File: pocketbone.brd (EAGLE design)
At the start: 55 x 35 mm, 61 parts, among them J1 USD_CONNECTOR, U5 24LC_32AT-I/OT, U6 SN74LVC1G07_DCK_5, Y1 CM200C-32.768KAZF-UT, Y2 445C33D24M00000

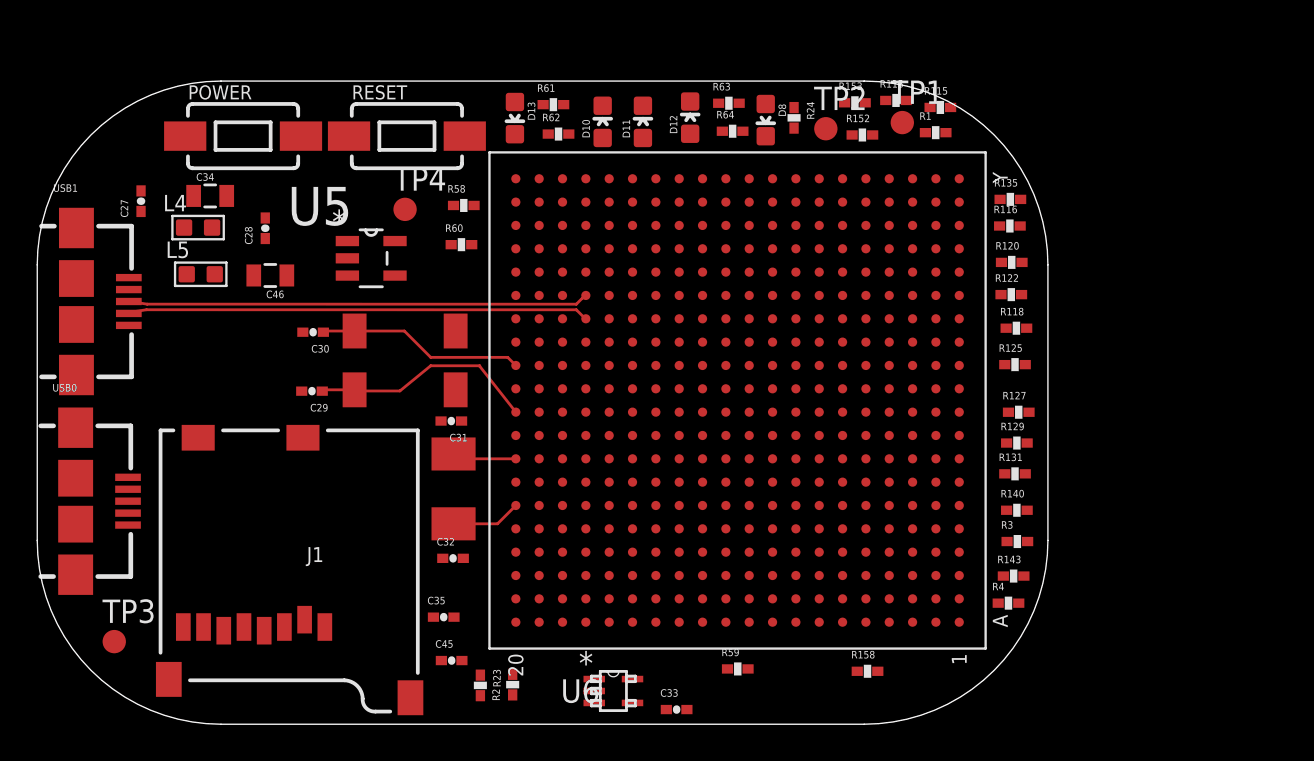
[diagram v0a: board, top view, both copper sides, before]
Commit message: Add ground plane
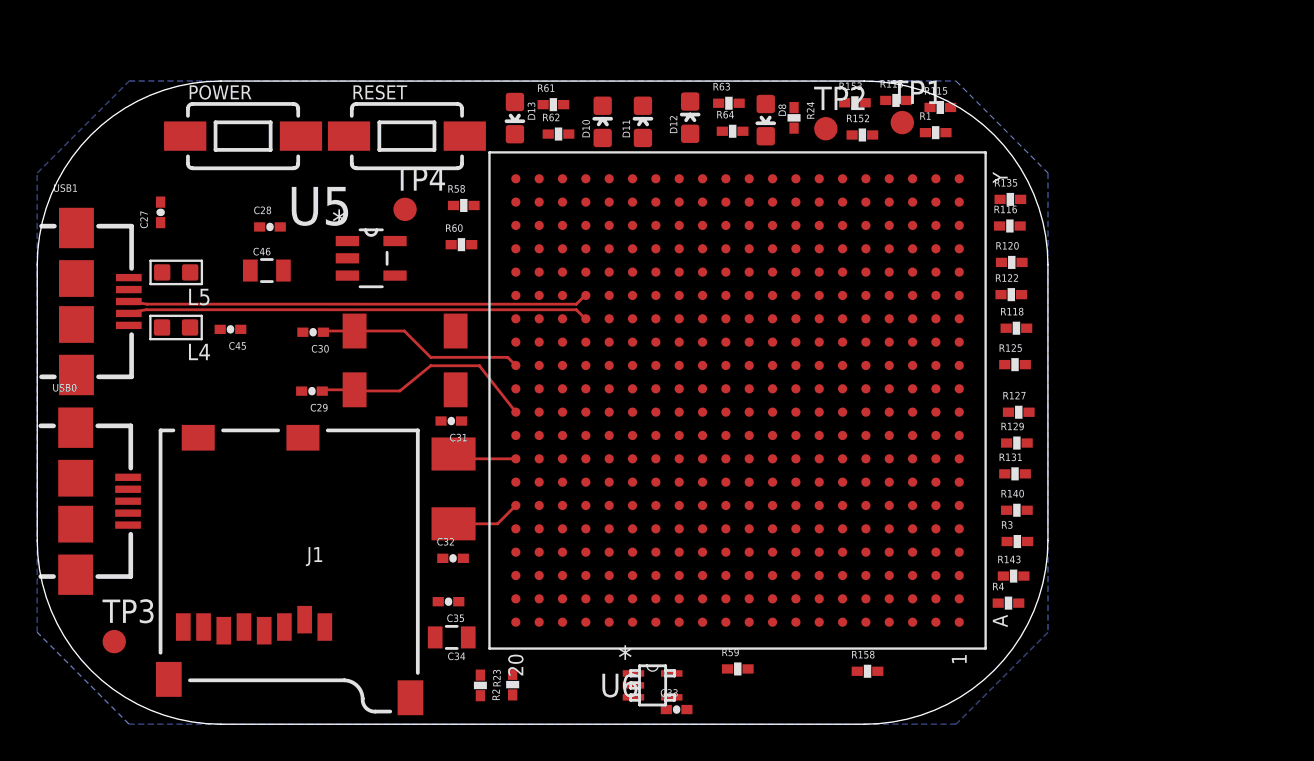
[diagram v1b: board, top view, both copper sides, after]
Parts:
- moved C34 27.4 mm to (22.6, 4.72), turned to 180 degrees
- moved C45 21.7 mm to (10.5, 21.5), turned to 180 degrees
- moved L4 5.57 mm to (7.55, 21.6), turned to 180 degrees
- moved U6 2.16 mm to (33.5, 2.11)
- moved L5 1.34 mm to (7.56, 24.6), turned to 180 degrees
- moved C27 1.23 mm to (6.71, 27.9)
- moved C35 0.88 mm to (22.4, 6.67), turned to 180 degrees
- moved C46 0.33 mm to (12.5, 24.7), turned to 0 degrees
- moved C28 0.26 mm to (12.7, 27.1), turned to 0 degrees
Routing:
- added copper zone on layer 16, net GND

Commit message: Consolidate library
* Renumber parts
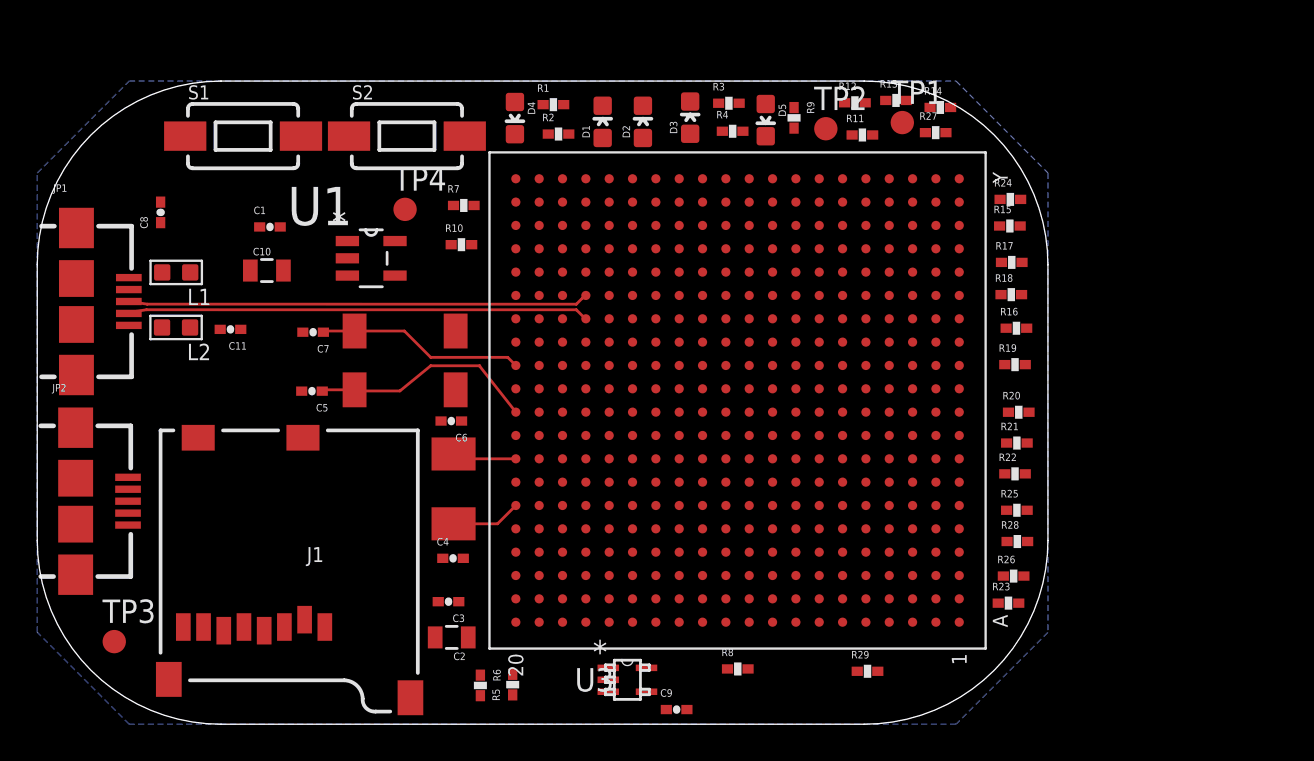
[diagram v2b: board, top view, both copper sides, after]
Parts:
- removed R135: 100K,1%, Strawson_Eagle_Lib:0402-RES
- removed R61, R62, R63, R64: 240, Strawson_Eagle_Lib:0402-RES
- removed SIP: OSD3358, BeagleBone_Blue:OSD3358
- removed U5: 24LC_32AT-I/OT, Microchip-24LCxxx:SOT95P290X145-5N
- removed U6: SN74LVC1G07_DCK_5, BeagleBone_Blue:DCK5
- removed USB0, USB1: USB-MICRO-SMD, Strawson_Eagle_Lib:USB-AB-MICRO-SMD
- added JP1, JP2: USB-MICRO-SMD, pocketbone:USB-AB-MICRO-SMD
- added R27, R28: 100K,1%, Strawson_Eagle_Lib:0402-RES
- added R5, R6: 1.5K,1%, Strawson_Eagle_Lib:0402-RES
- added R9: 4.87k, Strawson_Eagle_Lib:0402-RES
- added U1: 24LC_32AT-I/OT, pocketbone:SOT95P290X145-5N
- added U2: OSD3358, pocketbone:OSD3358
- added U3: SN74LVC1G07_DCK_5, pocketbone:DCK5
- J1: device BeagleBone_Blue:MICRO-SD-SOCKET-PP -> pocketbone:MICRO-SD-SOCKET-PP
- R1, R3, R4: value 100K,1% -> 240
- R2: value 1.5K,1% -> 240
- R23: value 1.5K,1% -> 100K,1%
- R24: value 4.87k -> 100K,1%
- Y1: value CM200C-32.768KAZF-UT -> 445C33D24M00000; device CM200C-32.768KAZF-UT:CM200C-32.768KAZF-UT -> pocketbone:445C33D24M00000
- Y2: value 445C33D24M00000 -> CM200C-32.768KAZF-UT; device 445C33D24M00000:445C33D24M00000 -> pocketbone:CM200C-32.768KAZF-UT
- moved R2 30.1 mm to (28.4, 32.1), turned to 0 degrees
- moved R4 29.7 mm to (37.8, 32.3)
- moved R23 29.1 mm to (52.9, 6.59), turned to 0 degrees
- moved R3 28.6 mm to (37.6, 33.8)
- moved R1 20.9 mm to (28.1, 33.7)
- moved R24 12.6 mm to (53.0, 28.6), turned to 0 degrees
- moved Y1 11.0 mm to (25.2, 9.64), turned to 90 degrees
- moved Y2 11.0 mm to (16.0, 15.7), turned to 0 degrees
- renumbered C27 to C8, C28 to C1, C29 to C5, C30 to C7, C31 to C6, C32 to C4, C33 to C9, C34 to C2, C35 to C3, C45 to C11, C46 to C10, D10 to D1, D11 to D2, D12 to D3, D13 to D4, D8 to D5, L4 to L2, L5 to L1, POWER to S1, R113 to R13, R115 to R14, R116 to R15, R118 to R16, R120 to R17, R122 to R18, R125 to R19, R127 to R20, R129 to R21, R131 to R22, R140 to R25, R143 to R26, R152 to R11, R153 to R12, R158 to R29, R58 to R7, R59 to R8, R60 to R10, RESET to S2
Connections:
- net 3.3V: now also R5.2, R6.2, U1.4, U2.U20, U2.V20; no longer R2.2, R23.2, SIP.U20, SIP.V20, U5.4
- net 5.0V: now also U2.Y5, U2.Y6; no longer SIP.Y5, SIP.Y6
- net BATT_LED_2: now also U2.T5; no longer SIP.T5
- net EQEP_1A: now also R27.2, U2.V2; no longer R1.2, SIP.V2
- net EQEP_1B: now also R28.2, U2.V3; no longer R3.2, SIP.V3
- net GND: now also JP2.GND, JP2.SHIELD1, JP2.SHIELD2, JP2.SHIELD3, JP2.SHIELD4, R2.1, R23.1, R24.1, R27.1, R28.1, R9.2, U1.2, U2.A1, U2.J6, U2.L19, U2.M10, U2.M19, U2.N7, U2.V1, U2.V19, U2.W11, U2.W2, U2.W20, U2.Y18, U3.3; no longer R135.1, R24.2, R61.1, R62.1, R63.1, R64.1, SIP.A1, SIP.J6, SIP.L19, SIP.M10, SIP.M19, SIP.N7, SIP.V1, SIP.V19, SIP.W11, SIP.W2, SIP.W20, SIP.Y18, U5.2, U6.3, USB0.GND, USB0.SHIELD1, USB0.SHIELD2, USB0.SHIELD3, USB0.SHIELD4
- net I2C0_SCL: now also R6.1, U1.1, U2.C16, U2.C20; no longer R23.1, SIP.C16, SIP.C20, U5.1
- net I2C0_SDA: now also R5.1, U1.3, U2.C17, U2.C19; no longer R2.1, SIP.C17, SIP.C19, U5.3
- net LCD_DATA_14: now also U2.V4; no longer SIP.V4
- net LDO_PGOOD: now also U2.B20, U2.B5; no longer SIP.B20, SIP.B5
- net MDIR_2B: now also R24.2, U2.U4; no longer R135.2, SIP.U4
- net MDIR_3A: now also U2.R4; no longer SIP.R4
- net MDIR_3B: now also U2.R3; no longer SIP.R3
- net MDIR_4A: now also U2.R1; no longer SIP.R1
- net MDIR_4B: now also U2.R2; no longer SIP.R2
- net N$1: now also JP1.VBUS; no longer USB1.VBUS
- net N$12: now also U2.C6, U2.D19; no longer SIP.C6, SIP.D19
- net N$128: now also JP1.GND, JP1.SHIELD1, JP1.SHIELD2, JP1.SHIELD3, JP1.SHIELD4; no longer USB1.GND, USB1.SHIELD1, USB1.SHIELD2, USB1.SHIELD3, USB1.SHIELD4
- net N$129: now also U2.T18; no longer SIP.T18
- net N$131: now also U2.B4; no longer SIP.B4
- net N$2: now also U2.G17; no longer SIP.G17
- net N$26: now also U2.M20, Y2.2; no longer SIP.M20, Y1.2
- net N$27: now also U2.K20, Y2.1; no longer SIP.K20, Y1.1
- net N$28: now also U1.5; no longer U5.5
- net N$31: now also U2.L20; no longer SIP.L20
- net N$32: now also U2.H20, Y1.2; no longer SIP.H20, Y2.2
- net N$33: now also U2.F20, Y1.1; no longer SIP.F20, Y2.1
- net N$34: now also U2.G20; no longer SIP.G20
- net N$42: now also U2.B10; no longer SIP.B10
- net N$43: now also U2.V16; no longer SIP.V16
- net N$44: now also U2.T15; no longer SIP.T15
- net N$45: now also U2.U15; no longer SIP.U15
- net N$46: now also U2.V15; no longer SIP.V15
- net N$47: now also R1.2; no longer R61.2
- net N$5: now also U2.F17; no longer SIP.F17
- net N$57: now also R2.2; no longer R62.2
- net N$58: now also R3.2; no longer R63.2
- net N$59: now also R4.2; no longer R64.2
- net N$70: now also U2.G15; no longer SIP.G15
- net N$74: now also U2.G18; no longer SIP.G18
- net N$75: now also U2.C15; no longer SIP.C15
- net N$77: now also U2.G16; no longer SIP.G16
- net NTE: now also U2.F18; no longer SIP.F18
- net PMIC_INT: now also U2.B18, U2.B19; no longer SIP.B18, SIP.B19
- net PMIC_NWAKEUP: now also U2.A19, U2.C5; no longer SIP.A19, SIP.C5
- net PMIC_PGOOD: now also U2.A20, U2.B15, U3.2; no longer SIP.A20, SIP.B15, U6.2
- net PWR: now also U2.D20; no longer SIP.D20
- net PWR_LEDR: now also R9.1; no longer R24.1
- net RESET: now also U2.A10, U3.4; no longer SIP.A10, U6.4
- net SERVO_EN: now also R23.2, U2.U3; no longer R4.2, SIP.U3
- net SVO5: now also U2.T3; no longer SIP.T3
- net SVO6: now also U2.T4; no longer SIP.T4
- net SVO7: now also U2.T1; no longer SIP.T1
- net SVO8: now also U2.T2; no longer SIP.T2
- net SYS_5V: now also U2.W4, U2.Y4; no longer SIP.W4, SIP.Y4
- net UART5_RX: now also U2.U2; no longer SIP.U2
- net UART5_TX: now also U2.U1; no longer SIP.U1
- net USB0_DM: now also JP2.D-, U2.N18; no longer SIP.N18, USB0.D-
- net USB0_DP: now also JP2.D+, U2.N17; no longer SIP.N17, USB0.D+
- net USB0_ID: now also JP2.ID, U2.P16; no longer SIP.P16, USB0.ID
- net USB1_DM: now also JP1.D-, U2.R18; no longer SIP.R18, USB1.D-
- net USB1_DP: now also JP1.D+, U2.R17; no longer SIP.R17, USB1.D+
- net USB1_ID: now also JP1.ID, U2.P17; no longer SIP.P17, USB1.ID
- net USB_DC: now also JP2.VBUS, U2.P15, U2.Y8, U2.Y9; no longer SIP.P15, SIP.Y8, SIP.Y9, USB0.VBUS
- net VDD_1V8: now also U2.D10, U2.E9, U2.N16, U2.R16; no longer SIP.D10, SIP.E9, SIP.N16, SIP.R16
- net VDD_3V3AUX: now also U2.Y11; no longer SIP.Y11
- net VDD_RTC: now also U2.E14, U3.5; no longer SIP.E14, U6.5
- net VIN_BAT_0: now also U2.Y2; no longer SIP.Y2
- net VIN_BAT_1: now also U2.Y3; no longer SIP.Y3
